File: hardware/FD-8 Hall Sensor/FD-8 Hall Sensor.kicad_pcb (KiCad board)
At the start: 2 copper layers, 27.9 x 45.7 mm, 22 parts, among them J1 Panel connections, J2 ICSP Programming, J3 Hall sensor input, J4 Extra GPIO, U1 LM2940T-5.0_NOPB, U2 ATtiny13A-P, U3 MCP42100

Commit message: use MCP42010 (both pots) instead of MCP42100
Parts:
- U3: value MCP42100 -> MCP42010
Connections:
- J1 pad 5: GND -> /PEDAL_SLEEVE
- U3 pad 10: GND -> Net-(U3-PA1)
- U3 pad 5: unconnected-(U3-PB1-Pad5) -> /PEDAL_SLEEVE
- U3 pad 6: unconnected-(U3-PW1-Pad6) -> Net-(U3-PA1)
- U3 pad 7: unconnected-(U3-PA1-Pad7) -> Net-(U3-PA1)
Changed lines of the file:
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@@
 	(net 11 "Net-(J4-Pin_1)")
 	(net 12 "unconnected-(U3-SO-Pad13)")
-	(net 13 "unconnected-(U3-PA1-Pad7)")
-	(net 14 "unconnected-(U3-PB1-Pad5)")
-	(net 15 "unconnected-(U3-PW1-Pad6)")
+	(net 13 "/PEDAL_SLEEVE")
+	(net 14 "Net-(U3-PA1)")
 	(footprint "Capacitor_THT:C_Disc_D4.3mm_W1.9mm_P5.00mm"
 		(layer "F.Cu")
@@
 			)
 		)
-		(property "Value" "MCP42100"
+		(property "Value" "MCP42010"
 			(at 3.81 17.57 0)
 			(layer "F.Fab")
@@
 			)
 		)
-		(property "Description" "Dual Digital Potentiometer, SPI interface, 256 taps, 100 kohm"
+		(property "Description" "Dual Digital Potentiometer, SPI interface, 256 taps, 10 kohm"
 			(at 0 0 0)
 			(layer "F.Fab")
@@
 			(layers "*.Cu" "*.Mask")
 			(remove_unused_layers no)
-			(net 14 "unconnected-(U3-PB1-Pad5)")
+			(net 13 "/PEDAL_SLEEVE")
 			(pinfunction "PB1")
-			(pintype "passive+no_connect")
+			(pintype "passive")
 		)
 		(pad "6" thru_hole circle
@@
 			(layers "*.Cu" "*.Mask")
 			(remove_unused_layers no)
-			(net 15 "unconnected-(U3-PW1-Pad6)")
+			(net 14 "Net-(U3-PA1)")
 			(pinfunction "PW1")
-			(pintype "passive+no_connect")
+			(pintype "passive")
 		)
 		(pad "7" thru_hole circle
@@
 			(layers "*.Cu" "*.Mask")
 			(remove_unused_layers no)
-			(net 13 "unconnected-(U3-PA1-Pad7)")
+			(net 14 "Net-(U3-PA1)")
 			(pinfunction "PA1")
-			(pintype "passive+no_connect")
+			(pintype "passive")
 		)
 		(pad "8" thru_hole circle
@@
 			(layers "*.Cu" "*.Mask")
 			(remove_unused_layers no)
-			(net 2 "GND")
+			(net 14 "Net-(U3-PA1)")
 			(pinfunction "PB0")
 			(pintype "passive")
@@
 			(layers "*.Cu" "*.Mask")
 			(remove_unused_layers no)
-			(net 2 "GND")
+			(net 13 "/PEDAL_SLEEVE")
 			(pinfunction "Pin_5")
 			(pintype "passive")

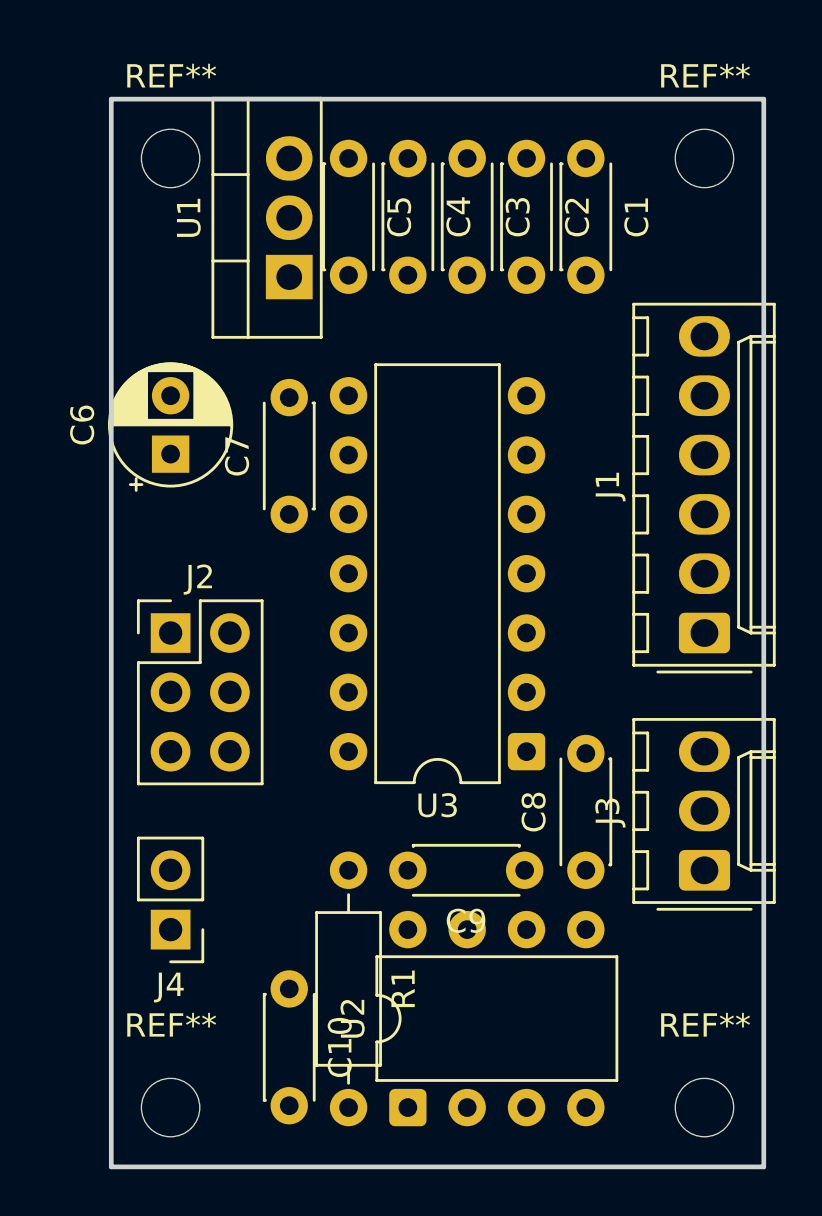
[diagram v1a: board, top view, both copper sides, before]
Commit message: fix caps; lock mounting holes
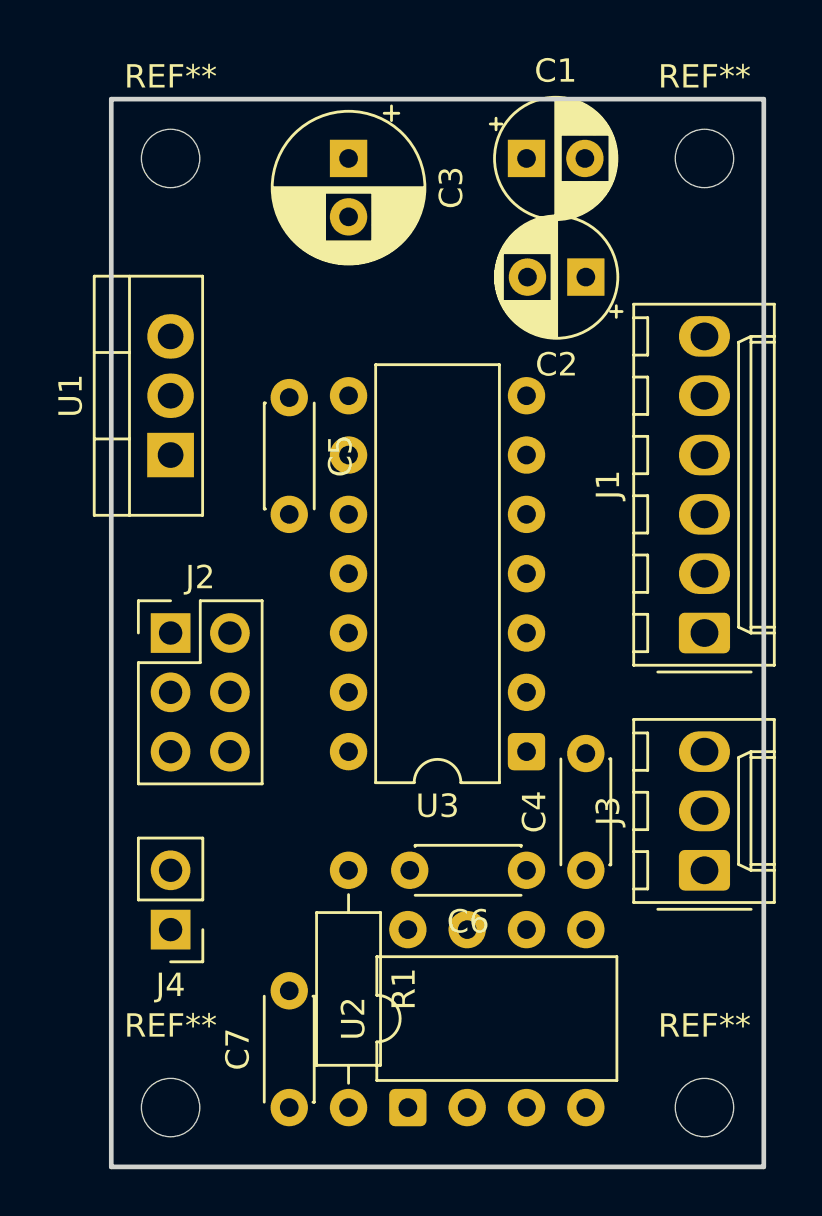
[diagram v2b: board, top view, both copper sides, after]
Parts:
- removed C10, C8, C9: 100nF, Capacitor_THT:C_Disc_D4.3mm_W1.9mm_P5.00mm
- C1, C2: value 100nF -> ~; footprint Capacitor_THT:C_Disc_D4.3mm_W1.9mm_P5.00mm -> Capacitor_THT:CP_Radial_D5.0mm_P2.50mm
- C3: value 100nF -> 100uF 25V; footprint Capacitor_THT:C_Disc_D4.3mm_W1.9mm_P5.00mm -> Capacitor_THT:CP_Radial_D6.3mm_P2.50mm
- C6: value 100uF 25V -> 100nF; footprint Capacitor_THT:CP_Radial_D5.0mm_P2.50mm -> Capacitor_THT:C_Disc_D4.3mm_W1.9mm_P5.00mm
- moved C4 31.4 mm to (195.6, 106.7), turned to 90 degrees
- moved C7 25.4 mm to (182.9, 116.8)
- moved C6 23.4 mm to (193.0, 106.7), turned to 180 degrees
- moved C5 10.6 mm to (182.9, 86.4)
- moved U1 9.16 mm to (177.8, 88.9)
- moved C2 5.68 mm to (195.6, 81.3), turned to 180 degrees
- moved C3 5.08 mm to (185.4, 76.2)
- moved C1 2.54 mm to (193.0, 76.2), turned to 0 degrees
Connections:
- C1 pad 2: GND -> Net-(C1-Pad2)
- C2 pad 1: Net-(J1-Pin_2) -> Net-(C1-Pad2)
- C3 pad 1: Net-(J1-Pin_2) -> +5V
- C4 pad 1: Net-(J1-Pin_2) -> +5V
- C5 pad 1: Net-(J1-Pin_2) -> +5V
- C7 pad 1: +5V -> /RESET

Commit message: routing etc.
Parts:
- moved U1 16.3 mm to (188.0, 76.2), turned to 0 degrees
- moved C3 9.18 mm to (180.3, 83.8), turned to 180 degrees
- moved C2 7.62 mm to (188.0, 81.3)
- moved C1 5.68 mm to (195.6, 81.3), turned to 180 degrees
- moved C5 5.00 mm to (182.9, 91.4), turned to 180 degrees
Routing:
- net /ICSP_MOSI: track 0.00 -> 39.6 mm
- net /ICSP_SCK: track 0.00 -> 27.5 mm
- net /ICSP_MISO: track 0.00 -> 27.0 mm
- net Net-(J1-Pin_2): track 0.00 -> 25.8 mm
- net /RESET: track 0.00 -> 22.4 mm
- net /PEDAL_TIP: track 0.00 -> 18.8 mm
- net Net-(J3-Pin_2): track 0.00 -> 15.9 mm
- net Net-(J4-Pin_1): track 0.00 -> 15.9 mm
- net Net-(U3-PA1): track 0.00 -> 11.2 mm
- net /PEDAL_SLEEVE: track 0.00 -> 9.72 mm
- net Net-(C1-Pad2): track 0.00 -> 5.12 mm
- added copper zone on In2.Cu, net +5V
- added copper zone on In1.Cu, net GND
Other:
- copper layers 2 -> 4
